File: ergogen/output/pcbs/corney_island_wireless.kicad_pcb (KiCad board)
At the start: 2 copper layers, 133.8 x 91.7 mm, 75 parts

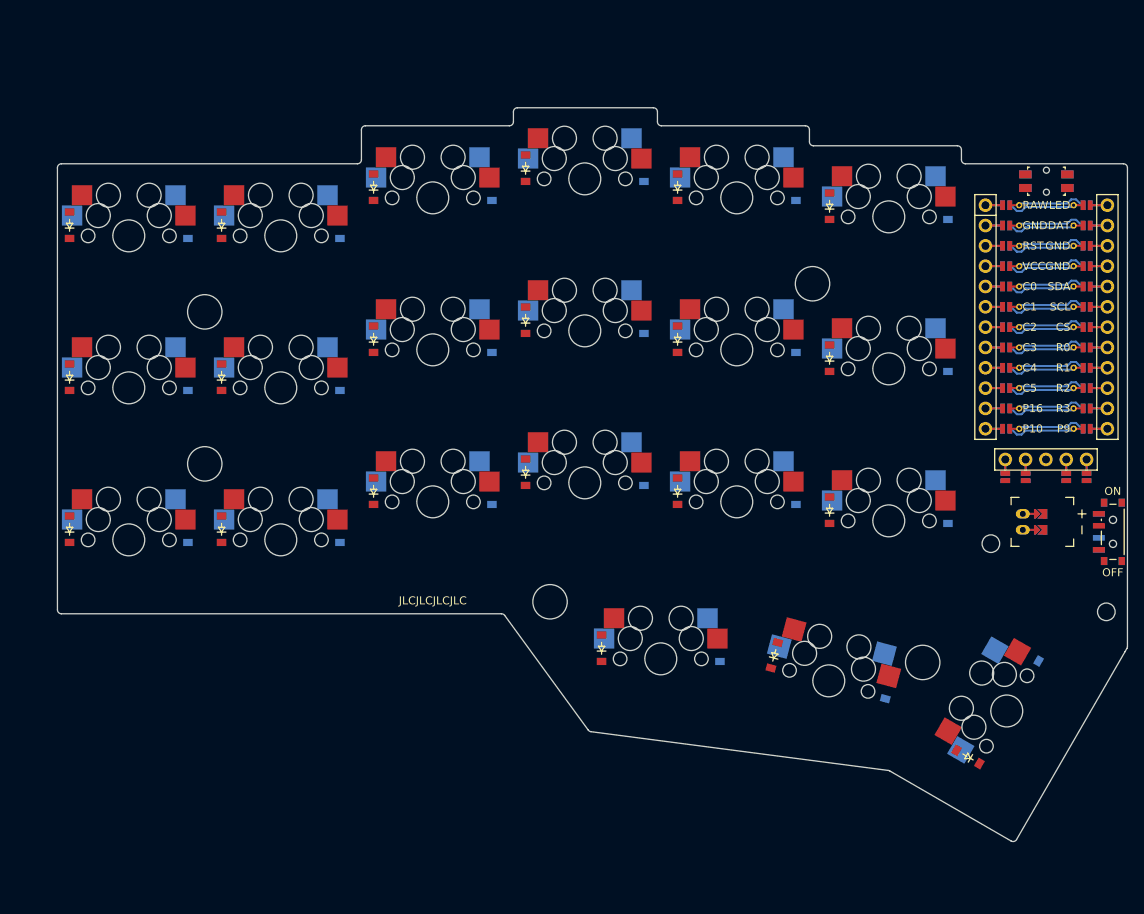
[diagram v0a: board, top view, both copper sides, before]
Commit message: Removed outer column
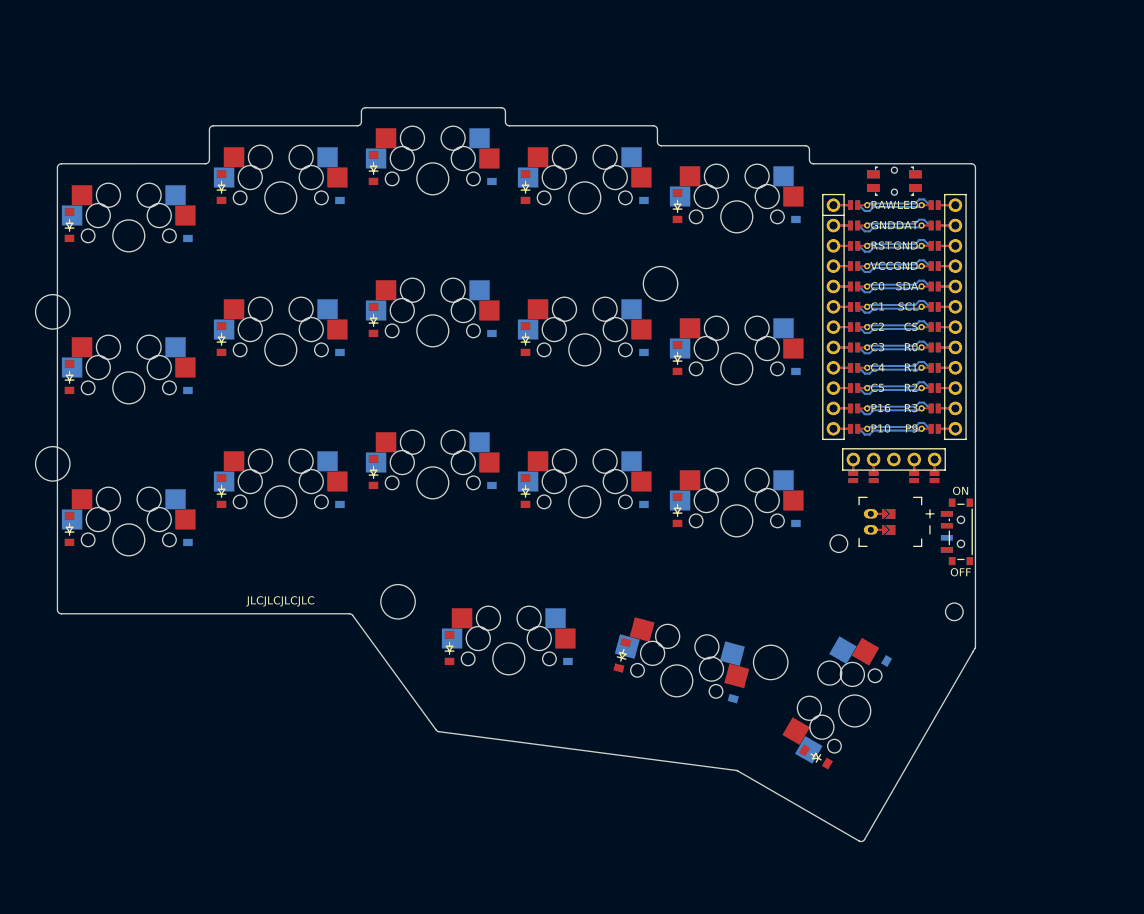
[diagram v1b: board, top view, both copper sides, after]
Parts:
- removed D37, D38, D39, D40, D41, D42: , ceoloide:diode_tht_sod123
- removed S19, S20, S21: , MX
- D19, D20, D21: moved to F.Cu
- moved D21 131.2 mm to (92.6, 60.7), turned to 90 degrees
- moved D20 109.4 mm to (92.6, 79.7), turned to 90 degrees
- moved D19 82.6 mm to (92.6, 98.7)
- moved D36 73.3 mm to (185.9, 127.1), turned to 150 degrees
- moved S18 61.9 mm to (190.7, 121.4), turned to 60 degrees
- moved D18 56.8 mm to (193.3, 114.3), turned to 150 degrees
- moved D16 50.5 mm to (154.9, 113.5)
- moved S16 50.5 mm to (147.5, 114.9)
- moved D17 48.7 mm to (176.0, 118.3), turned to 75 degrees
- moved S17 47.2 mm to (168.5, 117.6), turned to -15 degrees
- moved D35 40.1 mm to (161.7, 114.4), turned to 75 degrees
- moved D34 34.6 mm to (140.1, 113.5)
- moved D25 20.3 mm to (130.6, 91.5)
- moved D26 20.3 mm to (130.6, 72.5)
- moved D27 20.3 mm to (130.6, 53.5)
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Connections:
- D1 pad 2: outer_bottom -> pinky_bottom
- D10 pad 2: middle_bottom -> index_bottom
- D11 pad 2: middle_home -> index_home
- D12 pad 2: middle_top -> index_top
- D13 pad 2: index_bottom -> inner_bottom
- D14 pad 2: index_home -> inner_home
- D15 pad 2: index_top -> inner_top
- D16 pad 1: R2 -> R3
- D16 pad 2: inner_bottom -> near_home
- D17 pad 1: R1 -> R3
- D17 pad 2: inner_home -> mid_home
- D18 pad 1: R0 -> R3
- D18 pad 2: inner_top -> far_home
- D19 pad 1: R3 -> R2
- D19 pad 2: near_home -> pinky_bottom
- D2 pad 2: outer_home -> pinky_home
- D20 pad 1: R3 -> R1
- D20 pad 2: mid_home -> pinky_home
- D21 pad 1: R3 -> R0
- D21 pad 2: far_home -> pinky_top
- D22 pad 2: outer_bottom -> ring_bottom
- D23 pad 2: outer_home -> ring_home
- D24 pad 2: outer_top -> ring_top
- D25 pad 2: pinky_bottom -> middle_bottom
- D26 pad 2: pinky_home -> middle_home
- D27 pad 2: pinky_top -> middle_top
- D28 pad 2: ring_bottom -> index_bottom
- D29 pad 2: ring_home -> index_home
- D3 pad 2: outer_top -> pinky_top
- D30 pad 2: ring_top -> index_top
- D31 pad 2: middle_bottom -> inner_bottom
- D32 pad 2: middle_home -> inner_home
- D33 pad 2: middle_top -> inner_top
- D34 pad 1: R2 -> R3
- D34 pad 2: index_bottom -> near_home
- D35 pad 1: R1 -> R3
- D35 pad 2: index_home -> mid_home
- D36 pad 1: R0 -> R3
- D36 pad 2: index_top -> far_home
- D4 pad 2: pinky_bottom -> ring_bottom
- D5 pad 2: pinky_home -> ring_home
- D6 pad 2: pinky_top -> ring_top
- D7 pad 2: ring_bottom -> middle_bottom
- D8 pad 2: ring_home -> middle_home
- D9 pad 2: ring_top -> middle_top
- MCU1 pad 1: MCU1_1 -> LED
- MCU1 pad 10: MCU1_10 -> R2
- MCU1 pad 11: MCU1_11 -> R3
- MCU1 pad 12: MCU1_12 -> P9
- MCU1 pad 2: MCU1_2 -> DAT
- MCU1 pad 3: MCU1_3 -> GND
- MCU1 pad 4: MCU1_4 -> GND
- MCU1 pad 5: MCU1_5 -> SDA
- MCU1 pad 6: MCU1_6 -> SCL
- MCU1 pad 7: MCU1_7 -> CS
- MCU1 pad 8: MCU1_8 -> R0
- MCU1 pad 9: MCU1_9 -> R1
- S1 pad 1: C0 -> C1
- S1 pad 2: outer_bottom -> pinky_bottom
- S10 pad 1: C3 -> C4
- S10 pad 2: middle_bottom -> index_bottom
- S11 pad 1: C3 -> C4
- S11 pad 2: middle_home -> index_home
- S12 pad 1: C3 -> C4
- S12 pad 2: middle_top -> index_top
- S13 pad 1: C4 -> C5
- S13 pad 2: index_bottom -> inner_bottom
- S14 pad 1: C4 -> C5
- S14 pad 2: index_home -> inner_home
- S15 pad 1: C4 -> C5
- S15 pad 2: index_top -> inner_top
- S16 pad 1: C5 -> C3
- S16 pad 2: inner_bottom -> near_home
- S17 pad 1: C5 -> C4
- S17 pad 2: inner_home -> mid_home
- S18 pad 2: inner_top -> far_home
- S2 pad 1: C0 -> C1
- S2 pad 2: outer_home -> pinky_home
- S3 pad 1: C0 -> C1
- S3 pad 2: outer_top -> pinky_top
- S4 pad 1: C1 -> C2
- S4 pad 2: pinky_bottom -> ring_bottom
- S5 pad 1: C1 -> C2
- S5 pad 2: pinky_home -> ring_home
- S6 pad 1: C1 -> C2
- S6 pad 2: pinky_top -> ring_top
- S7 pad 1: C2 -> C3
- S7 pad 2: ring_bottom -> middle_bottom
- S8 pad 1: C2 -> C3
- S8 pad 2: ring_home -> middle_home
- S9 pad 1: C2 -> C3
- S9 pad 2: ring_top -> middle_top
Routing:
- net inner_top: track 0.00 -> 101.6 mm
- net pinky_bottom: track 0.00 -> 101.4 mm
- net far_home: track 0.00 -> 50.9 mm
- net R2: track 9.63 -> 50.9 mm
- net GND: track 28.9 -> 3.50 mm
- net C3: track 9.64 -> 0.00 mm
- net VCC: track 9.64 -> 0.00 mm
- net RST: track 9.64 -> 0.00 mm
- net RAW: track 9.64 -> 0.00 mm
- net C2: track 9.64 -> 0.00 mm
- net C0: track 9.64 -> 0.00 mm
- net P16: track 9.64 -> 0.00 mm
- net P10: track 9.64 -> 0.00 mm
- net C5: track 9.64 -> 0.00 mm
- net R3: track 9.63 -> 0.00 mm
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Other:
- board size 133.8 x 91.7 mm -> 114.8 x 91.7 mm

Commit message: Changed stagger to be like karia
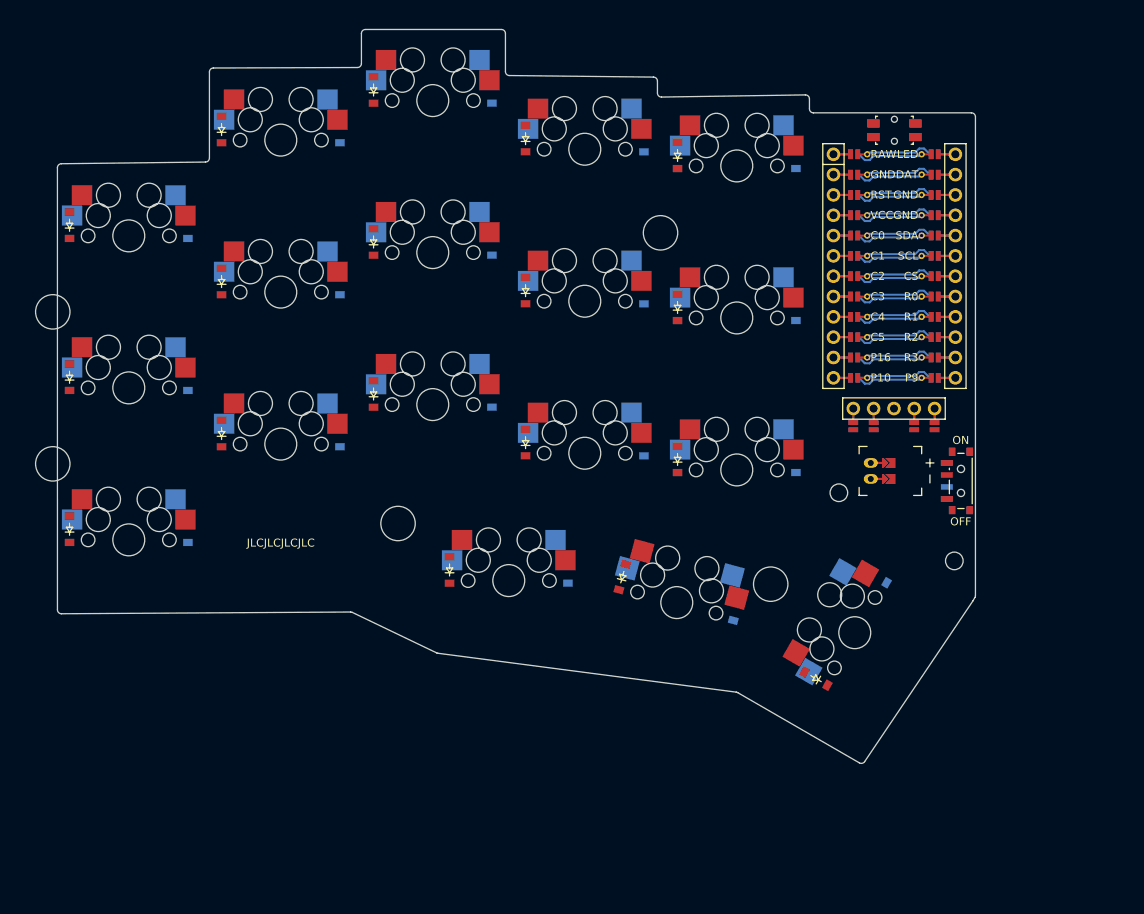
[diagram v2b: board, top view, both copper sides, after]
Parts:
- moved D16 9.78 mm to (154.9, 103.8)
- moved D17 9.78 mm to (176.0, 108.5)
- moved D18 9.78 mm to (193.3, 104.5)
- moved D25 9.78 mm to (130.6, 81.8)
- moved D26 9.78 mm to (130.6, 62.8)
- moved D27 9.78 mm to (130.6, 43.8)
- moved D34 9.78 mm to (140.1, 103.8)
- moved D35 9.78 mm to (161.7, 104.6)
- moved D36 9.78 mm to (185.9, 117.4)
- moved D7 9.78 mm to (145.4, 81.8)
- moved D8 9.78 mm to (145.4, 62.8)
- moved D9 9.78 mm to (145.4, 43.8)
- moved MH6 9.78 mm to (133.7, 98.0)
- moved MH7 9.78 mm to (180.2, 105.5)
- moved S16 9.78 mm to (147.5, 105.1)
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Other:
- outline, holes or cut-outs redrawn

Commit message: Added splay to pinky
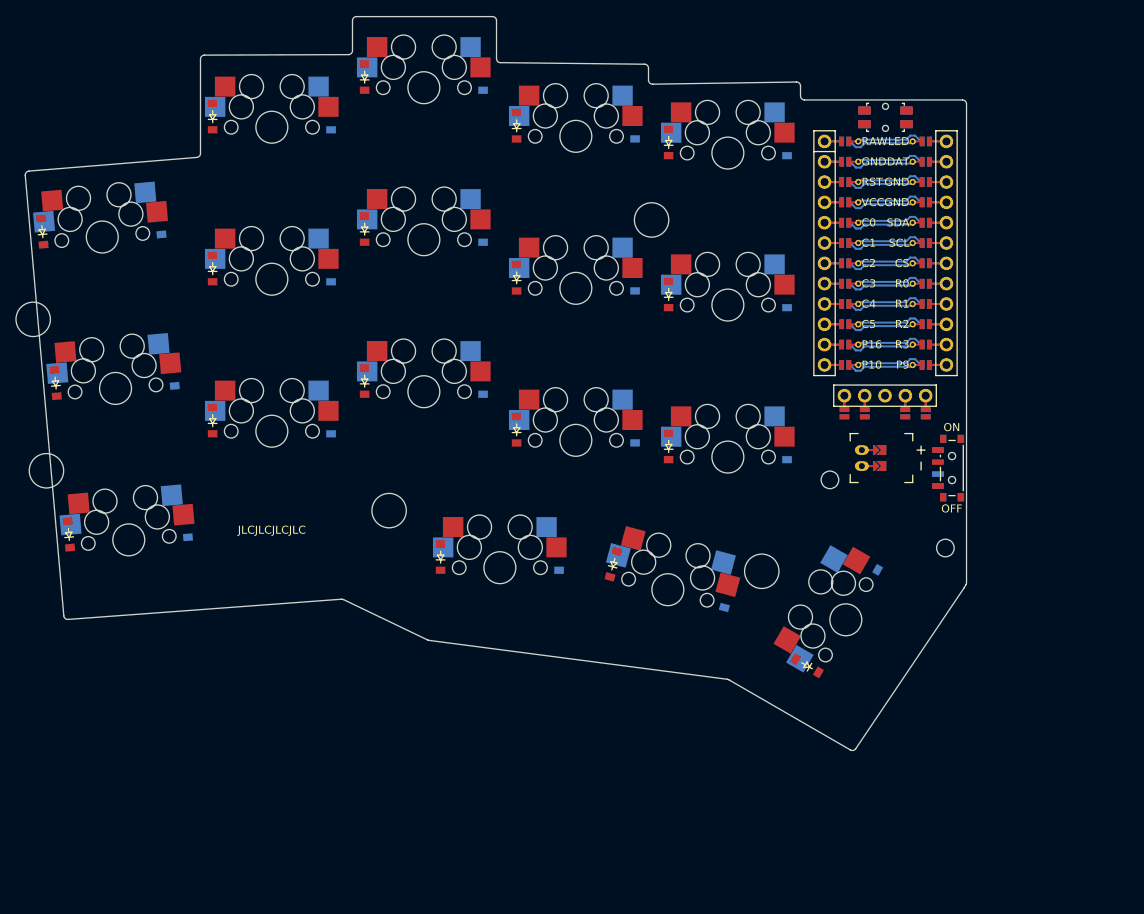
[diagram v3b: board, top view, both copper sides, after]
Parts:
- moved D3 3.49 mm to (103.9, 60.2), turned to 95 degrees
- moved D21 3.49 mm to (89.2, 61.5), turned to 95 degrees
- moved S3 3.32 mm to (96.7, 62.1), turned to 5 degrees
- moved MH3 2.62 mm to (88.1, 72.4), turned to 5 degrees
- moved D16 1.96 mm to (153.8, 102.2)
- moved D17 1.96 mm to (174.9, 106.9)
- moved D18 1.96 mm to (192.2, 102.9)
- moved D25 1.96 mm to (129.5, 80.2)
- moved D26 1.96 mm to (129.5, 61.2)
- moved D27 1.96 mm to (129.5, 42.2)
- moved D34 1.96 mm to (139.0, 102.2)
- moved D35 1.96 mm to (160.6, 103.0)
- moved D36 1.96 mm to (184.8, 115.7)
- moved D7 1.96 mm to (144.3, 80.2)
- moved D8 1.96 mm to (144.3, 61.2)
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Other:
- board size 114.8 x 91.7 mm -> 117.7 x 91.7 mm
